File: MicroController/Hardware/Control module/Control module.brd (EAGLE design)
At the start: 100 x 60 mm, 85 parts, among them IC1 MCP1703CB, J1 1X2-3.5MM, J2 RJ45-TRAFO, J3 RJ45-TRAFO, J4 RJ45-TRAFO, J6 RJ11, Q1 BSS138, Q10 BSS138, Q2 BSS138, Q3 BSS138, Q4 BSS138, Q5 BSS138, Q6 BSS138, Q7 BSS138, Q8 BSS138, Q9 BSS138, U1 CD74HC4067SM96, U2 7812DT, U3 TLV1117-33CDCY

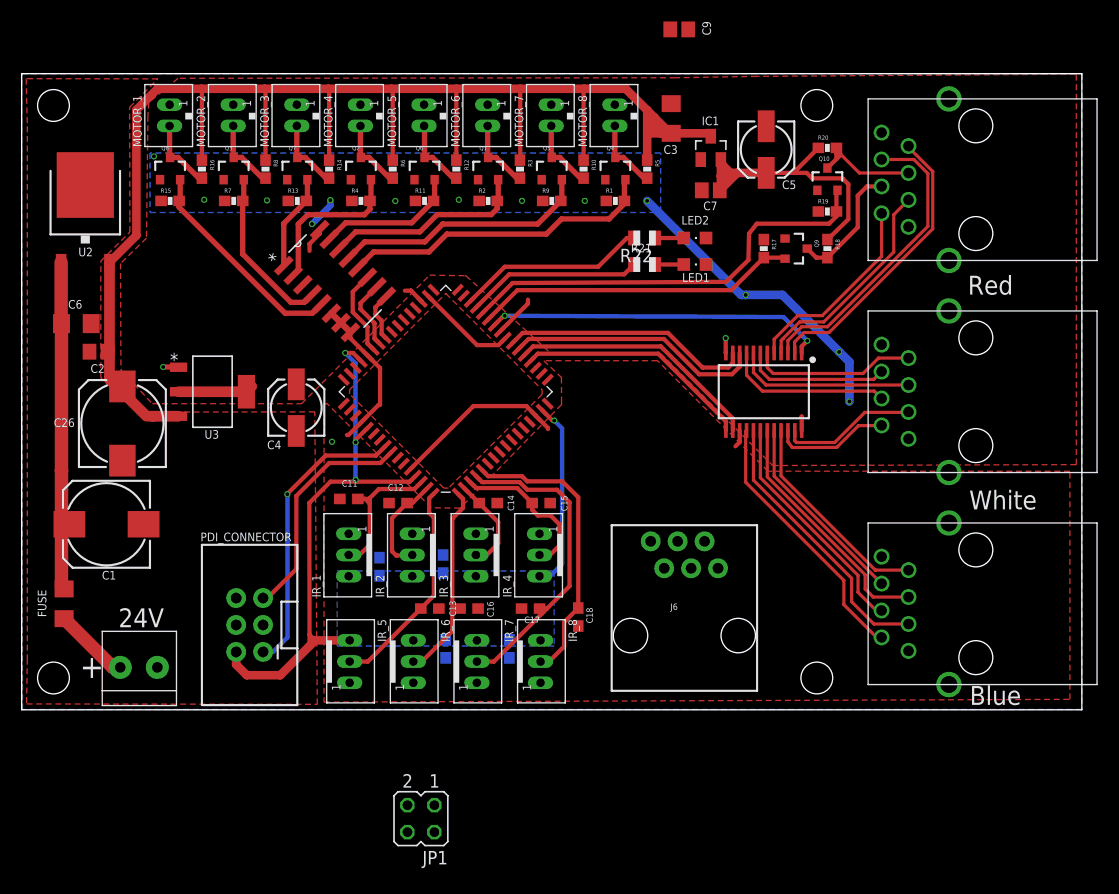
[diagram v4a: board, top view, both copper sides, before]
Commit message: Added the temperature sensors
Also changed a lot of connections and PCB traces.
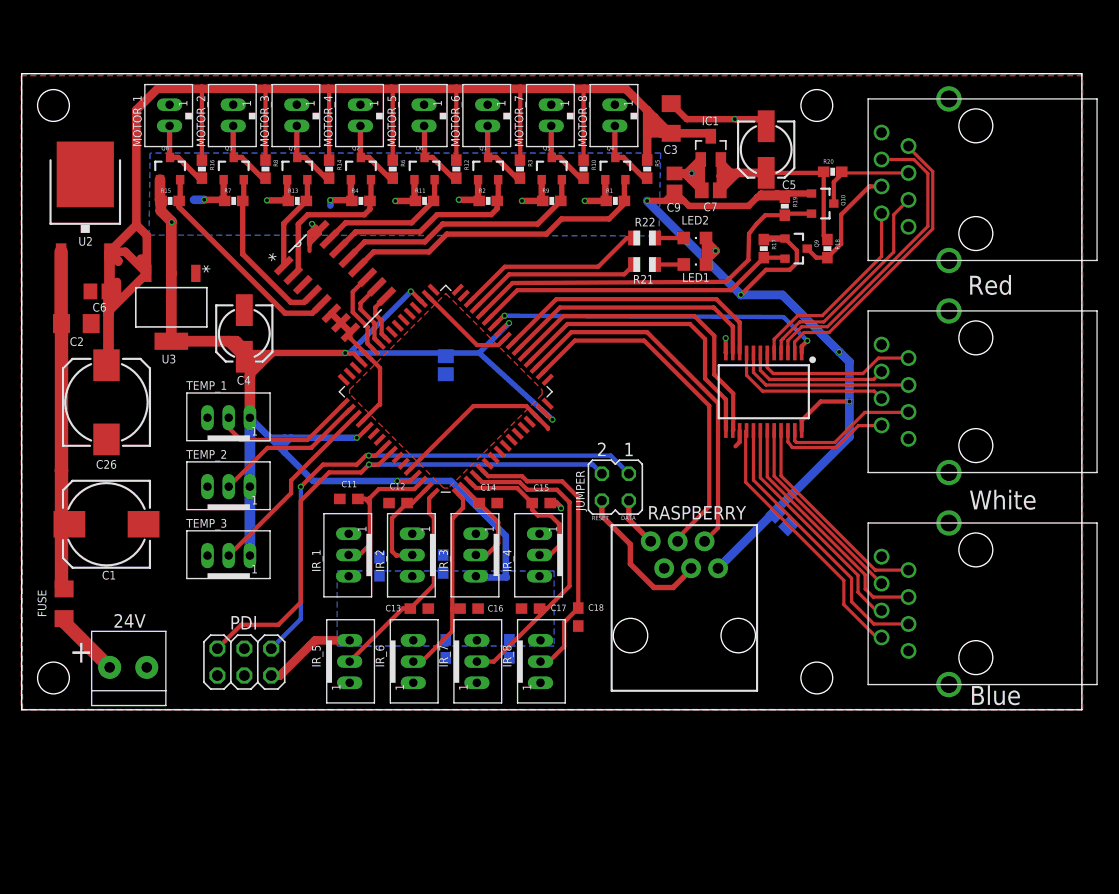
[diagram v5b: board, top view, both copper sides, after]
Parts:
- removed JP1: (no value), jumper:JP2Q
- removed PDI_CONNECTOR: (no value), SparkFun-Connectors:2X3-SHROUDED
- added C10, C8: (no value), adafruit:C0805
- added JUMPER: (no value), jumper:JP2Q
- added PDI: (no value), pinhead:2X03
- added TEMP_1, TEMP_2, TEMP_3: JST-PH_3-PIN_HEADER, SRG:JST_B3B-PH_HEADER
- moved C9 14.4 mm to (61.6, 49.7), turned to 90 degrees
- moved U3 8.86 mm to (14.1, 38.0), turned to 270 degrees
- moved C4 8.54 mm to (21.0, 35.5), turned to 270 degrees
- moved C6 5.69 mm to (7.34, 39.5)
- moved R19 4.05 mm to (72.0, 47.5), turned to 270 degrees
- moved C26 2.50 mm to (8.00, 29.0)
- moved Q10 2.30 mm to (75.5, 47.8), turned to 270 degrees
- moved R20 2.30 mm to (76.5, 50.8)
- moved C13 1.00 mm to (37.5, 9.55)
- moved J1 1.00 mm to (10.0, 4.00)
- moved U2 1.00 mm to (6.00, 48.0)
- renumbered J6 to RASPBERRY
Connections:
- removed net GND_RASPI: RASPBERRY.2
- removed net VCC_RASPI: RASPBERRY.6
- new net TEMP_1: TEMP_1.P2, U$1.49
- new net TEMP_2: TEMP_2.P2, U$1.50
- new net TEMP_3: TEMP_3.P2, U$1.51
- net DATA_RASPI: now also JUMPER.2, RASPBERRY.1; no longer JP1.2, RASPBERRY.5
- net GND: now also C10.2, C8.2, PDI.6, RASPBERRY.2, TEMP_1.P3, TEMP_2.P3, TEMP_3.P3; no longer PDI_CONNECTOR.6
- net PDI_DATA: now also JUMPER.1, PDI.1; no longer JP1.1, PDI_CONNECTOR.1
- net RESET_PDI_CLK: now also JUMPER.3, PDI.5; no longer JP1.3, PDI_CONNECTOR.5
- net RES_RASPI: now also JUMPER.4, RASPBERRY.4; no longer JP1.4, RASPBERRY.1
- net S0: now also U$1.23; no longer U$1.22
- net S1: now also U$1.22; no longer U$1.23
- net TX_ATXMEGA: now also RASPBERRY.5; no longer RASPBERRY.4
- net VCC: now also C10.1, C8.1, PDI.2, RASPBERRY.6, TEMP_1.P1, TEMP_2.P1, TEMP_3.P1; no longer PDI_CONNECTOR.2
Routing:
- net VCC: track 122.5 -> 287.7 mm, vias 17 -> 19
- net TX_ATXMEGA: track 0.01 -> 34.9 mm
- net RX_ATXMEGA: track 0.00 -> 33.7 mm
- net RESET_PDI_CLK: track 21.9 -> 52.1 mm, vias 0 -> 1
- net GND: track 45.4 -> 69.9 mm, vias 3 -> 5
- net PDI_DATA: track 27.6 -> 51.3 mm, vias 1 -> 2
- net TEMP_3: track 0.00 -> 18.2 mm
- net RES_RASPI: track 0.00 -> 14.6 mm
- net TEMP_2: track 0.00 -> 14.4 mm
- net TEMP_1: track 0.00 -> 13.7 mm
- net +12V: track 148.1 -> 158.2 mm
- net S2: track 24.0 -> 30.0 mm
- net S3: track 22.3 -> 28.0 mm
- net +5V: track 28.9 -> 23.3 mm
- net ATXMEGA_TRIGGER_1: track 41.2 -> 36.4 mm
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- added copper zone on layer 1, net +12V
- removed copper zone on layer 1, net VCC
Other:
- board text added: "DATA"
- board text added: "RESET"

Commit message: Added the hardware that makes the TTL line of a higher voltage.
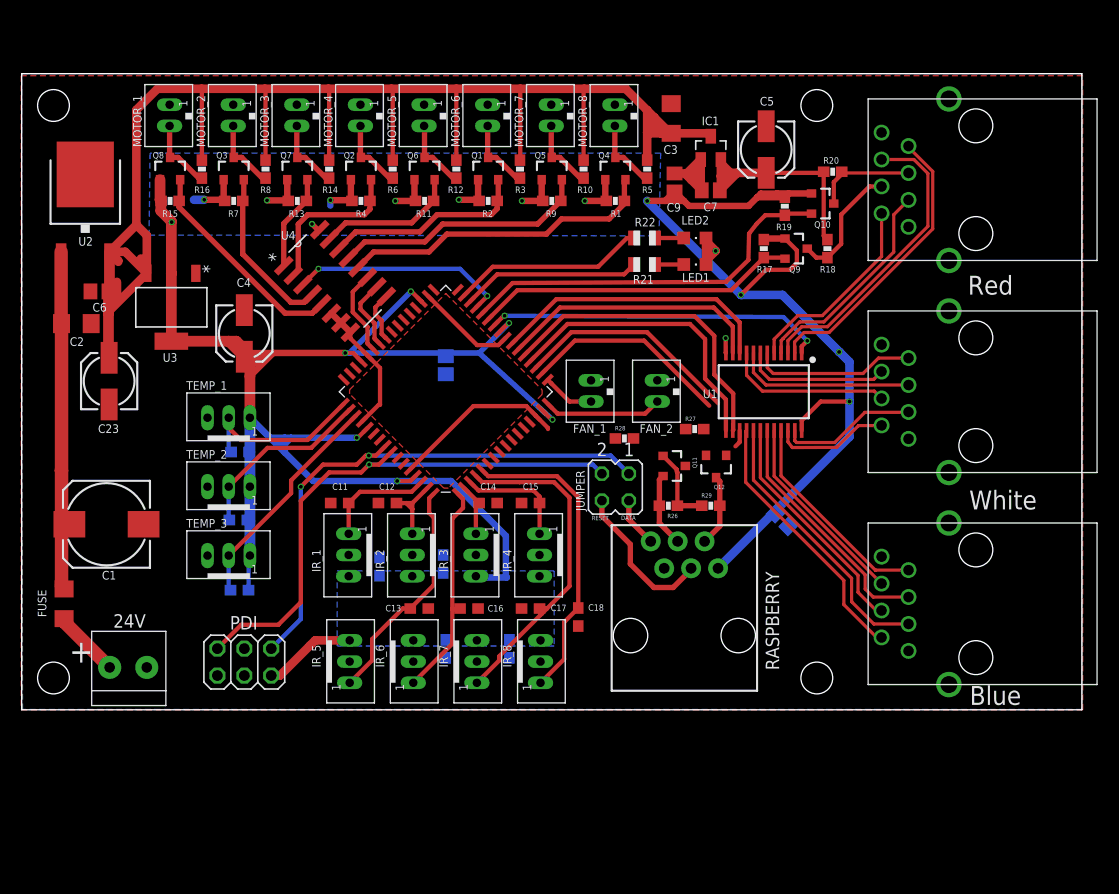
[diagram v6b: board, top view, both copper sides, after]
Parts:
- removed C26: (no value), adafruit:175TMP-0810
- added C23: 22uF, adafruit:153CLV-0505
- added FAN_1, FAN_2: JST-PH_2-PIN_HEADER, SRG:JST_B2B-PH_HEADER
- added Q11, Q12: BSS138, SparkFun:SOT23-3
- added R23, R24, R25: 4K7, SparkFun:0603-RES
- added R26, R27, R28, R29: 10K, SparkFun:0603-RES
- C1: value (none) -> 220uF
- C10, C11, C12, C13, C14, C15, C16, C17, C18, C19, C20, C21, C22, C3, C6, C7, C8, C9: value (none) -> 100nF
- C2: value (none) -> 220pF
- C4, C5: value (none) -> 22uF
- R21, R22: value 10K -> 330
- moved C12 1.00 mm to (34.5, 19.5)
- moved C15 1.00 mm to (48.0, 19.5), turned to 180 degrees
- moved C11 0.95 mm to (30.0, 19.5)
- renumbered MOTOR_CONTROL_DEMULTIPLEXER to U4
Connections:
- net ATXMEGA_TRIGGER_1 renamed ULTRA_TRIGGER_1
- net ATXMEGA_TRIGGER_2 renamed ULTRA_TRIGGER_2
- new net FAN_1_CONTROL: FAN_1.P2, U$1.17
- new net FAN_2_CONTROL: FAN_2.P2, U$1.16
- new net RX_RASPI: Q12.3, R29.2, RASPBERRY.5
- new net TX_RASPI: Q11.2, R26.2, RASPBERRY.3
- net +12V: now also C23.+, Q11.1, R26.1, R29.1; no longer C26.+
- net GND: now also C23.-, FAN_1.P1, FAN_2.P1, IR_1.P2, IR_2.P2, IR_3.P2, IR_4.P2, IR_5.P2, IR_6.P2, IR_7.P2, IR_8.P2; no longer C26.-, IR_1.P1, IR_2.P1, IR_3.P1, IR_4.P1, IR_5.P1, IR_6.P1, IR_7.P1, IR_8.P1
- net IR_1: now also IR_1.P1; no longer IR_1.P2
- net IR_2: now also IR_2.P1; no longer IR_2.P2
- net IR_3: now also IR_3.P1; no longer IR_3.P2
- net IR_4: now also IR_4.P1; no longer IR_4.P2
- net IR_5: now also IR_5.P1; no longer IR_5.P2
- net IR_6: now also IR_6.P1; no longer IR_6.P2
- net IR_7: now also IR_7.P1; no longer IR_7.P2
- net IR_8: now also IR_8.P1; no longer IR_8.P2
- net LED_1: now also U$1.30; no longer U$1.29
- net LED_2: now also U$1.31; no longer U$1.30
- net MOTOR_CONTROL: now also U$1.29
- net RX_ATXMEGA: now also Q11.3, R27.2; no longer RASPBERRY.3
- net TEMP_1: now also R23.2
- net TEMP_2: now also R24.2
- net TEMP_3: now also R25.2
- net TX_ATXMEGA: now also Q12.2, R28.2; no longer RASPBERRY.5
- net VCC: now also Q12.1, R23.1, R24.1, R25.1, R27.1, R28.1
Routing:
- net MOTOR_CONTROL: track 0.00 -> 20.7 mm, vias 0 -> 2
- net RX_ATXMEGA: track 33.7 -> 19.6 mm
- net TX_ATXMEGA: track 34.9 -> 21.4 mm
- net GND: track 69.9 -> 56.9 mm, vias 5 -> 2
- net FAN_2_CONTROL: track 0.00 -> 11.2 mm
- net +12V: track 158.2 -> 165.8 mm
- net TX_RASPI: track 0.00 -> 7.02 mm
- net RX_RASPI: track 0.00 -> 6.75 mm
- net FAN_1_CONTROL: track 0.00 -> 4.94 mm
- net IR_1: track 14.8 -> 10.6 mm
- net IR_3: track 9.17 -> 5.08 mm
- net IR_4: track 14.7 -> 10.7 mm
- net TEMP_1: track 13.7 -> 17.0 mm
- net TEMP_3: track 18.2 -> 21.5 mm
- net TEMP_2: track 14.4 -> 17.6 mm
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
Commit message: Changed some minor things to make the PCB less expensive to produce.
Also the RX TX is now of a higher voltage. This should make the communication less susceptible to noise.
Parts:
- moved R28 6.91 mm to (63.8, 26.0)
- moved R27 4.26 mm to (59.2, 26.0)
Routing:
- net +12V: track 165.8 -> 225.6 mm, vias 0 -> 2
- net VCC: track 287.1 -> 312.3 mm, vias 19 -> 20
- net RX_ATXMEGA: track 19.6 -> 28.2 mm
- net TX_ATXMEGA: track 21.4 -> 26.8 mm
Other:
- board text added: "Bidon Dispenser 4.0"
- board text added: "Control PCB 1.0"
- board text added: "Glen te Hofsté"

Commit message: The version that is ordered at Eurocircuits.
The full version of the microcontroller PCB, revision 1.
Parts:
- J2, J3, J4: value RJ45-TRAFO -> 0446200002; device con-amphenol-rj45-ld:RJ45-TRAFO -> con-molex:0446200002
- moved RASPBERRY 1.50 mm to (62.5, 5.50)
- moved J3 0.75 mm to (90.0, 10.8)
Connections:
- net GND: now also J2.S@1, J2.S@2, J3.S@1, J3.S@2, J4.S@1, J4.S@2; no longer J2.GND1, J2.GND2, J3.GND1, J3.GND2, J4.GND1, J4.GND2
- net TRIGGER_1: now also J4.4; no longer J4.5
- net TRIGGER_2: now also J4.5; no longer J4.4
- net ULTRA1: now also J2.2; no longer J2.7
- net ULTRA10: now also J4.6; no longer J4.2
- net ULTRA11: now also J3.2; no longer J3.7
- net ULTRA12: now also J3.3; no longer J3.6
- net ULTRA13: now also J3.4; no longer J3.5
- net ULTRA14: now also J3.5; no longer J3.4
- net ULTRA15: now also J3.6; no longer J3.3
- net ULTRA16: now also J3.7; no longer J3.2
- net ULTRA2: now also J2.3; no longer J2.6
- net ULTRA3: now also J2.4; no longer J2.5
- net ULTRA4: now also J2.5; no longer J2.4
- net ULTRA5: now also J2.6; no longer J2.3
- net ULTRA6: now also J2.7; no longer J2.2
- net ULTRA7: now also J4.2; no longer J4.7
- net ULTRA8: now also J4.3; no longer J4.6
- net ULTRA9: now also J4.7; no longer J4.3
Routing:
- net ULTRA6: track 11.0 -> 18.8 mm
- net ULTRA4: track 15.7 -> 21.6 mm
- net ULTRA2: track 13.7 -> 19.6 mm
- net ULTRA7: track 27.3 -> 32.5 mm
- net TRIGGER_2: track 11.8 -> 16.5 mm
- net ULTRA12: track 18.6 -> 23.2 mm
- net ULTRA14: track 22.0 -> 25.6 mm
- net ULTRA10: track 18.7 -> 21.8 mm
- net ULTRA16: track 25.1 -> 28.1 mm
- net ULTRA5: track 13.0 -> 15.2 mm
- net TRIGGER_1: track 9.59 -> 11.8 mm
- net ULTRA3: track 17.0 -> 18.8 mm
- net RES_RASPI: track 14.6 -> 16.4 mm
- net ULTRA9: track 20.8 -> 22.4 mm
- net DATA_RASPI: track 4.69 -> 6.19 mm
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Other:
- board size 100 x 60 mm -> 95 x 60 mm
- board text added: "U1"
